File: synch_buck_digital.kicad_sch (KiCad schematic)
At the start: 48 parts, among them U1 BSC066N06NSATMA1, U2 BSC066N06NSATMA1, U3 INA241A3IDDFR

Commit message: update
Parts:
- added R1: 0R, symbol Device:R_US
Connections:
- net COMP_OUT: now also J_STM1.2 (Pin_8); no longer J_STM1.8 (Pin_8)
- net DT_REF: now also J_STM1.1 (Pin_3); no longer J_STM1.3 (Pin_3)
- net PGND: now also R1.1; no longer C_DT_100P1.2, C_DT_10N1.2, C_DT_1U1.2, C_INA_FILT2.1, C_INA_FILT3.1, C_INA_VCC1.2, C_OC_100P1.2, C_OC_10N1.2, C_OC_1U1.2, C_VFB_FILT1.1, D1.2 (A), J_STM1.10 (Pin_10), J_STM1.11 (Pin_11), J_STM1.12 (Pin_12), J_STM1.13 (Pin_13), R1_DT1.2, R1_VFB1.1, R_HYS1.1, R_HYS2.1, TP1.1, U3.2 (GND), U3.3 (REF2), U3.4 (NC), U3.7 (REF1), U_DT1.2 (VEE), U_OC1.2 (VEE), U_UCC1.7 (VSS)
- net PROT_OUT: now also J_STM1.3 (Pin_5); no longer J_STM1.5 (Pin_5)
- net PWM_HS: now also J_STM1.6 (Pin_7); no longer J_STM1.7 (Pin_7)
- net PWM_LS: now also J_STM1.5 (Pin_1); no longer J_STM1.1 (Pin_1)
- net SENSE_OUT: now also J_STM1.7 (Pin_6); no longer J_STM1.6 (Pin_6)
- net V_FB: now also J_STM1.8 (Pin_2); no longer J_STM1.2 (Pin_2)
- new net SGND: C_DT_100P1.2, C_DT_10N1.2, C_DT_1U1.2, C_INA_FILT2.1, C_INA_FILT3.1, C_INA_VCC1.2, C_OC_100P1.2, C_OC_10N1.2, C_OC_1U1.2, C_VFB_FILT1.1, D1.2 (A), J_STM1.10 (Pin_10), J_STM1.11 (Pin_11), J_STM1.12 (Pin_12), J_STM1.13 (Pin_13), R1.2, R1_DT1.2, R1_VFB1.1, R_HYS1.1, R_HYS2.1, TP1.1, U3.2 (GND), U3.3 (REF2), U3.4 (NC), U3.7 (REF1), U_DT1.2 (VEE), U_OC1.2 (VEE), U_UCC1.7 (VSS)
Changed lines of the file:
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@@
 	(symbol
 		(lib_id "power:GND")
-		(at 198.12 208.28 90)
+		(at 201.93 208.28 90)
 		(mirror x)
 		(unit 1)
@@
 		(fields_autoplaced yes)
 		(property "Reference" "#PWR013"
-			(at 204.47 208.28 0)
+			(at 208.28 208.28 0)
 			(hide yes)
 			(show_name no)
@@
 		)
 		(property "Value" "SGND"
-			(at 201.93 208.2801 90)
+			(at 205.74 208.2801 90)
 			(show_name no)
 			(do_not_autoplace no)
@@
 		)
 		(property "Footprint" ""
-			(at 198.12 208.28 0)
+			(at 201.93 208.28 0)
 			(hide yes)
 			(show_name no)
@@
 		)
 		(property "Datasheet" ""
-			(at 198.12 208.28 0)
+			(at 201.93 208.28 0)
 			(hide yes)
 			(show_name no)
@@
 		)
 		(property "Description" "Power symbol creates a global label with name \"GND\" , ground"
-			(at 198.12 208.28 0)
+			(at 201.93 208.28 0)
 			(hide yes)
 			(show_name no)
@@
 	)
 	(symbol
+		(lib_id "Device:R_US")
+		(at 198.12 208.28 90)
+		(unit 1)
+		(body_style 1)
+		(exclude_from_sim no)
+		(in_bom yes)
+		(on_board yes)
+		(in_pos_files yes)
+		(dnp no)
+		(property "Reference" "R1"
+			(at 198.12 211.074 90)
+			(show_name no)
+			(do_not_autoplace no)
+			(effects
+				(font
+					(size 1.27 1.27)
+				)
+			)
+		)
+		(property "Value" "0R"
+			(at 198.12 213.106 90)
+			(show_name no)
+			(do_not_autoplace no)
+			(effects
+				(font
+					(size 1.27 1.27)
+				)
+			)
+		)
+		(property "Footprint" ""
+			(at 198.374 207.264 90)
+			(hide yes)
+			(show_name no)
+			(do_not_autoplace no)
+			(effects
+				(font
+					(size 1.27 1.27)
+				)
+			)
+		)
+		(property "Datasheet" ""
+			(at 198.12 208.28 0)
+			(hide yes)
+			(show_name no)
+			(do_not_autoplace no)
+			(effects
+				(font
+					(size 1.27 1.27)
+				)
+			)
+		)
+		(property "Description" "Resistor, US symbol"
+			(at 198.12 208.28 0)
+			(hide yes)
+			(show_name no)
+			(do_not_autoplace no)
+			(effects
+				(font
+					(size 1.27 1.27)
+				)
+			)
+		)
+		(pin "1"
+		)
+		(pin "2"
+		)
+		(instances
+			(project "synch_buck_digital"
+				(path "/9ffc6758-015a-4fde-b1f2-cf26f16b4b89"
+					(reference "R1")
+					(unit 1)
+				)
+			)
+		)
+	)
+	(symbol
 		(lib_id "Device:C")
 		(at 157.48 64.77 0)
@@
 	(symbol
 		(lib_id "power:GND")
-		(at 198.12 208.28 270)
+		(at 194.31 208.28 270)
 		(mirror x)
 		(unit 1)
@@
 		(fields_autoplaced yes)
 		(property "Reference" "#PWR014"
-			(at 191.77 208.28 0)
+			(at 187.96 208.28 0)
 			(hide yes)
 			(show_name no)
@@
 		)
 		(property "Value" "PGND"
-			(at 194.31 208.2801 90)
+			(at 190.5 208.2801 90)
 			(show_name no)
 			(do_not_autoplace no)
@@
 		)
 		(property "Footprint" ""
-			(at 198.12 208.28 0)
+			(at 194.31 208.28 0)
 			(hide yes)
 			(show_name no)
@@
 		)
 		(property "Datasheet" ""
-			(at 198.12 208.28 0)
+			(at 194.31 208.28 0)
 			(hide yes)
 			(show_name no)
@@
 		)
 		(property "Description" "Power symbol creates a global label with name \"GND\" , ground"
-			(at 198.12 208.28 0)
+			(at 194.31 208.28 0)
 			(hide yes)
 			(show_name no)

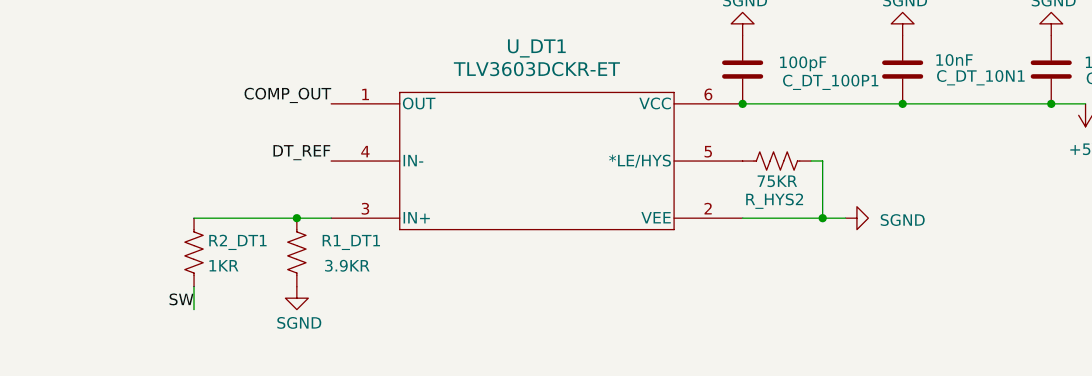
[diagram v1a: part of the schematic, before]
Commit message: pouring topology started
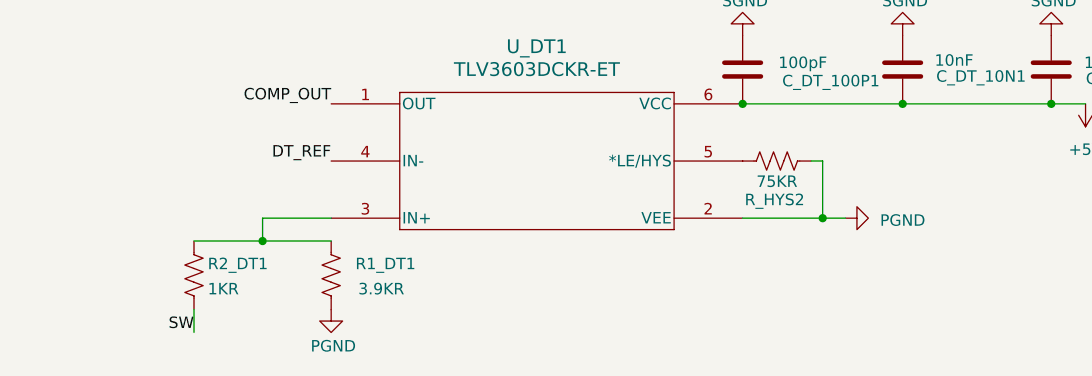
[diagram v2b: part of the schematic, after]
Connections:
- net PGND: now also R1_DT1.2, R_HYS2.1, U_DT1.2 (VEE)
- net SGND: no longer R1_DT1.2, R_HYS2.1, U_DT1.2 (VEE)
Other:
- moved on the sheet: R1_DT1, R2_DT1
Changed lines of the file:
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@@
 	)
 	(junction
-		(at 287.02 204.47)
-		(diameter 0)
-		(color 0 0 0 0)
-	)
-	(junction
 		(at 336.55 156.21)
 		(diameter 0)
@@
 	)
 	(junction
+		(at 283.21 207.01)
+		(diameter 0)
+		(color 0 0 0 0)
+	)
+	(junction
 		(at 157.48 60.96)
 		(diameter 0)
@@
 	(wire
 		(pts
+			(xy 290.83 204.47) (xy 283.21 204.47)
+		)
+		(stroke
+			(width 0)
+			(type default)
+		)
+	)
+	(wire
+		(pts
 			(xy 341.63 113.03) (xy 334.01 113.03)
 		)
@@
 	(wire
 		(pts
-			(xy 287.02 204.47) (xy 290.83 204.47)
-		)
-		(stroke
-			(width 0)
-			(type default)
-		)
-	)
-	(wire
-		(pts
 			(xy 170.18 129.54) (xy 180.34 129.54)
 		)
@@
 	(wire
 		(pts
+			(xy 283.21 207.01) (xy 290.83 207.01)
+		)
+		(stroke
+			(width 0)
+			(type default)
+		)
+	)
+	(wire
+		(pts
 			(xy 176.53 57.15) (xy 177.8 57.15)
 		)
@@
 	(wire
 		(pts
-			(xy 275.59 204.47) (xy 287.02 204.47)
-		)
-		(stroke
-			(width 0)
-			(type default)
-		)
-	)
-	(wire
-		(pts
 			(xy 176.53 85.09) (xy 177.8 85.09)
 		)
@@
 	(wire
 		(pts
+			(xy 283.21 204.47) (xy 283.21 207.01)
+		)
+		(stroke
+			(width 0)
+			(type default)
+		)
+	)
+	(wire
+		(pts
 			(xy 116.84 152.4) (xy 114.3 152.4)
 		)
@@
 	(wire
 		(pts
-			(xy 275.59 214.63) (xy 275.59 212.09)
+			(xy 275.59 217.17) (xy 275.59 214.63)
+		)
+		(stroke
+			(width 0)
+			(type default)
+		)
+	)
+	(wire
+		(pts
+			(xy 275.59 207.01) (xy 283.21 207.01)
 		)
 		(stroke
@@
 	)
 	(label "SW"
-		(at 275.59 214.63 180)
+		(at 275.59 217.17 180)
 		(effects
 			(font
@@
 	(symbol
 		(lib_id "Device:R_US")
-		(at 275.59 208.28 180)
+		(at 275.59 210.82 180)
 		(unit 1)
 		(body_style 1)
@@
 		(dnp no)
 		(property "Reference" "R2_DT1"
-			(at 277.114 207.01 0)
+			(at 277.114 209.55 0)
 			(show_name no)
 			(do_not_autoplace no)
@@
 		)
 		(property "Value" "1KR"
-			(at 277.114 209.8041 0)
+			(at 277.114 212.3441 0)
 			(show_name no)
 			(do_not_autoplace no)
@@
 		)
 		(property "Footprint" "Resistor_SMD:R_0603_1608Metric"
-			(at 274.574 208.026 90)
+			(at 274.574 210.566 90)
 			(hide yes)
 			(show_name no)
@@
 		)
 		(property "Datasheet" ""
-			(at 275.59 208.28 0)
+			(at 275.59 210.82 0)
 			(hide yes)
 			(show_name no)
@@
 		)
 		(property "Description" "Resistor, US symbol"
-			(at 275.59 208.28 0)
+			(at 275.59 210.82 0)
 			(hide yes)
 			(show_name no)
@@
 			)
 		)
-		(property "Value" "SGND"
+		(property "Value" "PGND"
 			(at 354.33 204.724 90)
 			(show_name no)
@@
 	(symbol
 		(lib_id "power:GND")
-		(at 287.02 212.09 0)
+		(at 290.83 214.63 0)
 		(unit 1)
 		(body_style 1)
@@
 		(dnp no)
 		(property "Reference" "#PWR022"
-			(at 287.02 218.44 0)
+			(at 290.83 220.98 0)
 			(hide yes)
 			(show_name no)
@@
 			)
 		)
-		(property "Value" "SGND"
-			(at 284.734 216.154 0)
+		(property "Value" "PGND"
+			(at 288.544 218.694 0)
 			(show_name no)
 			(do_not_autoplace no)
@@
 		)
 		(property "Footprint" ""
-			(at 287.02 212.09 0)
+			(at 290.83 214.63 0)
 			(hide yes)
 			(show_name no)
@@
 		)
 		(property "Datasheet" ""
-			(at 287.02 212.09 0)
+			(at 290.83 214.63 0)
 			(hide yes)
 			(show_name no)
@@
 		)
 		(property "Description" "Power symbol creates a global label with name \"GND\" , ground"
-			(at 287.02 212.09 0)
+			(at 290.83 214.63 0)
 			(hide yes)
 			(show_name no)
@@
 	(symbol
 		(lib_id "Device:R_US")
-		(at 287.02 208.28 0)
+		(at 290.83 210.82 0)
 		(unit 1)
 		(body_style 1)
@@
 		(dnp no)
 		(property "Reference" "R1_DT1"
-			(at 296.418 207.01 0)
+			(at 300.228 209.55 0)
 			(show_name no)
 			(do_not_autoplace no)
@@
 		)
 		(property "Value" "3.9KR"
-			(at 295.148 209.804 0)
+			(at 298.958 212.344 0)
 			(show_name no)
 			(do_not_autoplace no)
@@
 		)
 		(property "Footprint" "Resistor_SMD:R_0603_1608Metric"
-			(at 288.036 208.534 90)
+			(at 291.846 211.074 90)
 			(hide yes)
 			(show_name no)
@@
 		)
 		(property "Datasheet" ""
-			(at 287.02 208.28 0)
+			(at 290.83 210.82 0)
 			(hide yes)
 			(show_name no)
@@
 		)
 		(property "Description" "Resistor, US symbol"
-			(at 287.02 208.28 0)
+			(at 290.83 210.82 0)
 			(hide yes)
 			(show_name no)

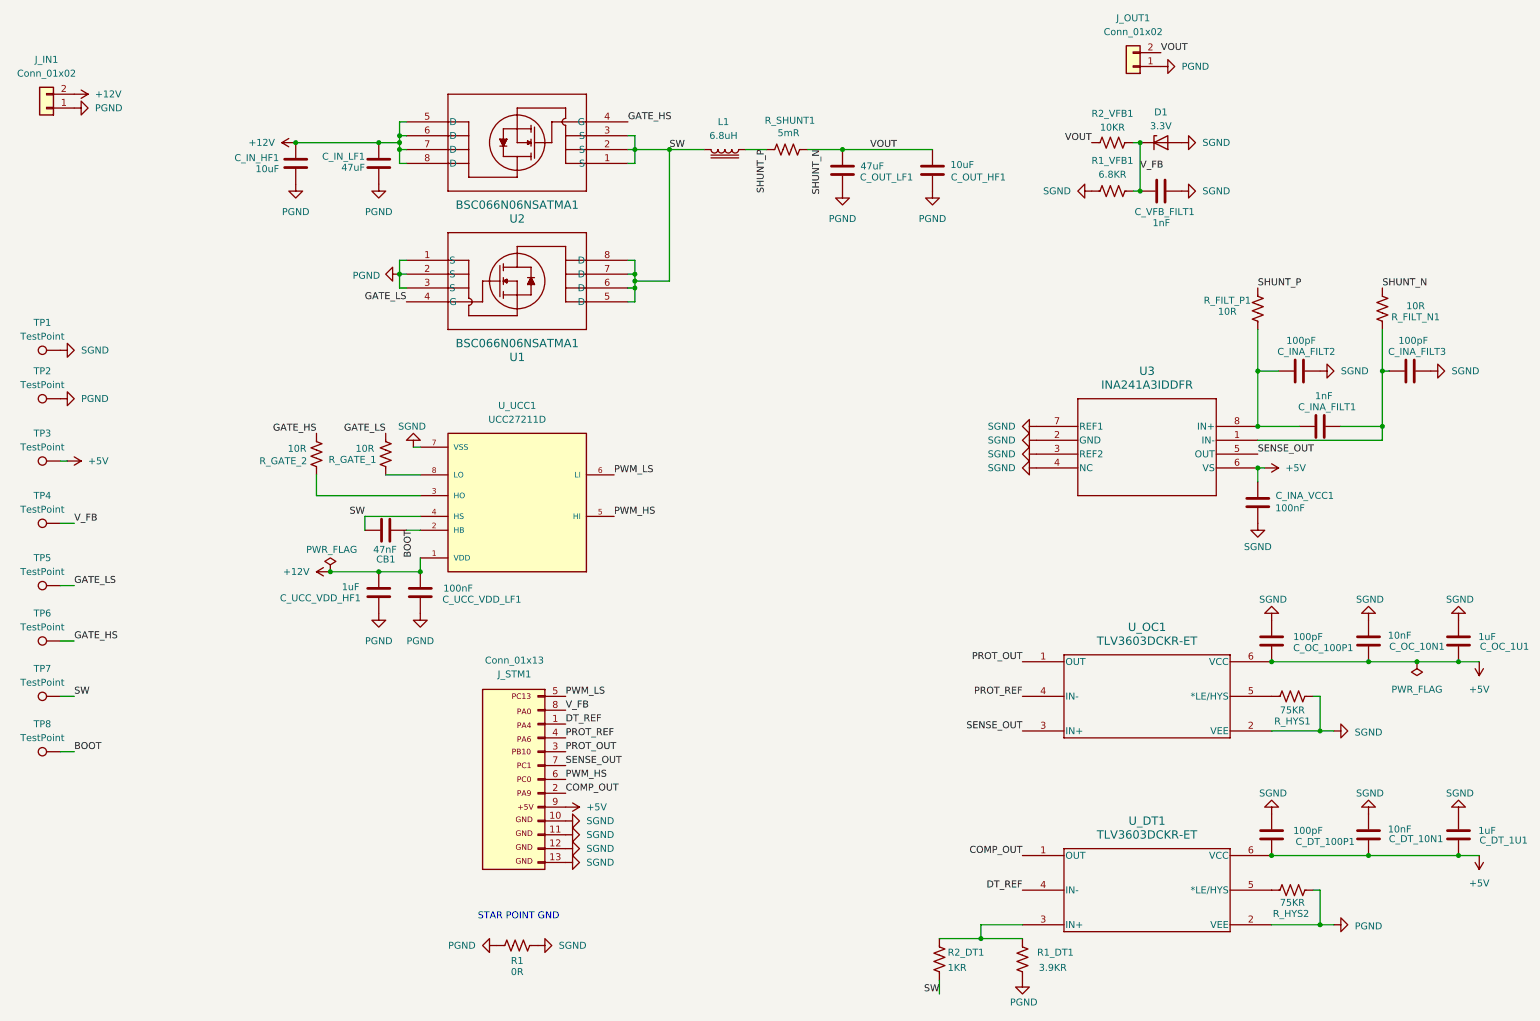
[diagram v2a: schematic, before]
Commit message: Added stitching and thermal pours
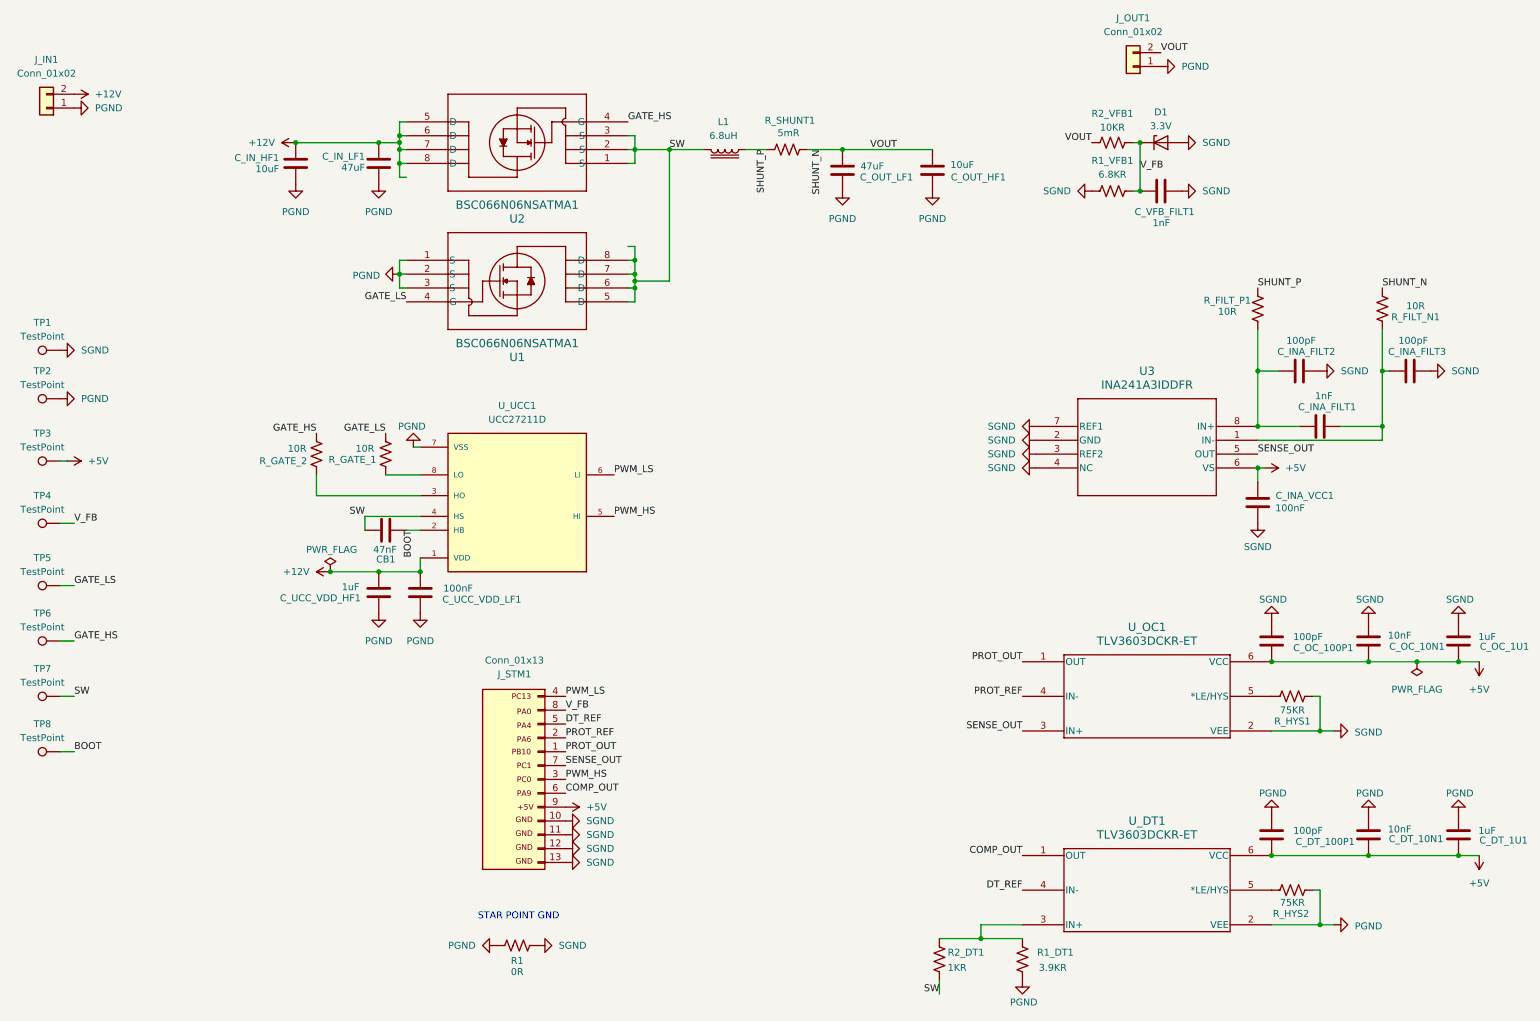
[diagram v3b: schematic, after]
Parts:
- U1, U2: footprint FET:PG-TDSON-8_INF -> PG-TDSON-8_INF
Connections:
- net COMP_OUT: now also J_STM1.6 (Pin_8); no longer J_STM1.2 (Pin_8)
- net DT_REF: now also J_STM1.5 (Pin_3); no longer J_STM1.1 (Pin_3)
- net PGND: now also C_DT_100P1.2, C_DT_10N1.2, C_DT_1U1.2, U_UCC1.7 (VSS)
- net PROT_OUT: now also J_STM1.1 (Pin_5); no longer J_STM1.3 (Pin_5)
- net PROT_REF: now also J_STM1.2 (Pin_4); no longer J_STM1.4 (Pin_4)
- net PWM_HS: now also J_STM1.3 (Pin_7); no longer J_STM1.6 (Pin_7)
- net PWM_LS: now also J_STM1.4 (Pin_1); no longer J_STM1.5 (Pin_1)
- net SGND: no longer C_DT_100P1.2, C_DT_10N1.2, C_DT_1U1.2, U_UCC1.7 (VSS)
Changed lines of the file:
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@@
 	)
 	(junction
+		(at 219.71 82.55)
+		(diameter 0)
+		(color 0 0 0 0)
+	)
+	(junction
 		(at 370.84 156.21)
 		(diameter 0)
@@
 	)
 	(junction
+		(at 176.53 64.77)
+		(diameter 0)
+		(color 0 0 0 0)
+	)
+	(junction
 		(at 363.22 156.21)
 		(diameter 0)
@@
 	(wire
 		(pts
+			(xy 219.71 80.01) (xy 219.71 82.55)
+		)
+		(stroke
+			(width 0)
+			(type default)
+		)
+	)
+	(wire
+		(pts
 			(xy 176.53 59.69) (xy 177.8 59.69)
 		)
@@
 	(wire
 		(pts
+			(xy 218.44 80.01) (xy 219.71 80.01)
+		)
+		(stroke
+			(width 0)
+			(type default)
+		)
+	)
+	(wire
+		(pts
 			(xy 219.71 85.09) (xy 218.44 85.09)
 		)
@@
 	(wire
 		(pts
+			(xy 177.8 67.31) (xy 176.53 67.31)
+		)
+		(stroke
+			(width 0)
+			(type default)
+		)
+	)
+	(wire
+		(pts
 			(xy 219.71 86.36) (xy 219.71 87.63)
 		)
@@
 	(wire
 		(pts
+			(xy 176.53 67.31) (xy 176.53 64.77)
+		)
+		(stroke
+			(width 0)
+			(type default)
+		)
+	)
+	(wire
+		(pts
 			(xy 312.42 60.96) (xy 311.15 60.96)
 		)
@@
 			)
 		)
-		(property "Value" "SGND"
+		(property "Value" "PGND"
 			(at 368.554 180.34 0)
 			(show_name no)
@@
 			)
 		)
-		(property "Value" "SGND"
+		(property "Value" "PGND"
 			(at 176.276 113.03 0)
 			(show_name no)
@@
 			)
 		)
-		(property "Value" "SGND"
+		(property "Value" "PGND"
 			(at 352.044 180.34 0)
 			(show_name no)
@@
 			)
 		)
-		(property "Value" "SGND"
+		(property "Value" "PGND"
 			(at 334.264 180.34 0)
 			(show_name no)
@@
 			)
 		)
-		(property "Footprint" "FET:PG-TDSON-8_INF"
+		(property "Footprint" "PG-TDSON-8_INF"
 			(at 177.8 82.55 0)
 			(hide yes)
@@
 		(pin "7"
 		)
+		(pin "9"
+		)
 		(instances
 			(project "synch_buck_digital"
@@
 			)
 		)
-		(property "Footprint" "FET:PG-TDSON-8_INF"
+		(property "Footprint" "PG-TDSON-8_INF"
 			(at 218.44 64.77 0)
 			(hide yes)
@@
 		(pin "5"
 		)
+		(pin "9"
+		)
 		(instances

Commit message: Small fix
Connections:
- net +12V: now also U2.9 (EP)
- net PGND: now also R2_DT1.1; no longer R1_DT1.2
- net SW: now also R1_DT1.2, U1.9 (EP); no longer R2_DT1.1
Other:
- moved on the sheet: R1_DT1, R2_DT1
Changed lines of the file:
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@@
 	(symbol
 		(lib_id "Device:R_US")
-		(at 275.59 210.82 180)
+		(at 290.83 210.82 180)
 		(unit 1)
 		(body_style 1)
@@
 		(dnp no)
 		(property "Reference" "R2_DT1"
-			(at 277.114 209.55 0)
+			(at 292.354 209.55 0)
 			(show_name no)
 			(do_not_autoplace no)
@@
 		)
 		(property "Value" "1KR"
-			(at 277.114 212.3441 0)
+			(at 292.354 212.3441 0)
 			(show_name no)
 			(do_not_autoplace no)
@@
 		)
 		(property "Footprint" "Resistor_SMD:R_0603_1608Metric"
-			(at 274.574 210.566 90)
+			(at 289.814 210.566 90)
 			(hide yes)
 			(show_name no)
@@
 		)
 		(property "Datasheet" ""
-			(at 275.59 210.82 0)
+			(at 290.83 210.82 0)
 			(hide yes)
 			(show_name no)
@@
 		)
 		(property "Description" "Resistor, US symbol"
-			(at 275.59 210.82 0)
+			(at 290.83 210.82 0)
 			(hide yes)
 			(show_name no)
@@
 	(symbol
 		(lib_id "Device:R_US")
-		(at 290.83 210.82 0)
+		(at 275.59 210.82 0)
 		(unit 1)
 		(body_style 1)
@@
 		(dnp no)
 		(property "Reference" "R1_DT1"
-			(at 300.228 209.55 0)
+			(at 284.988 209.55 0)
 			(show_name no)
 			(do_not_autoplace no)
@@
 		)
 		(property "Value" "3.9KR"
-			(at 298.958 212.344 0)
+			(at 283.718 212.344 0)
 			(show_name no)
 			(do_not_autoplace no)
@@
 		)
 		(property "Footprint" "Resistor_SMD:R_0603_1608Metric"
-			(at 291.846 211.074 90)
+			(at 276.606 211.074 90)
 			(hide yes)
 			(show_name no)
@@
 		)
 		(property "Datasheet" ""
-			(at 290.83 210.82 0)
+			(at 275.59 210.82 0)
 			(hide yes)
 			(show_name no)
@@
 		)
 		(property "Description" "Resistor, US symbol"
-			(at 290.83 210.82 0)
+			(at 275.59 210.82 0)
 			(hide yes)
 			(show_name no)

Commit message: V1 finished. Final touchups to schematic planned
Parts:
- U1, U2: footprint PG-TDSON-8_INF -> Package_SON:Infineon_PG-TDSON-8_6.15x5.15mm
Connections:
- net +12V: no longer U2.6 (D), U2.7 (D), U2.8 (D), U2.9 (EP)
- net SW: no longer U1.6 (D), U1.7 (D), U1.8 (D), U1.9 (EP)
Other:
- moved on the sheet: C_IN_HF1, C_IN_LF1
